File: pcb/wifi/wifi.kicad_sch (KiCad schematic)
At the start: 0 parts

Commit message: big components placed
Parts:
- added U1: ESP32-H2, PCM_Espressif:QFN-32-1EP_4x4mm_P0.4mm_EP2.9x2.9mm, symbol Espressif:ESP32-H2
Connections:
- new net: U1.1 (VDD3P3), U1.2 (VDD3P3), U1.27 (VDD3P3), U1.30 (VDD3P3), U1.31 (VDD3P3)
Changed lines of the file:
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@@
 	(generator_version "10.0")
 	(paper "A4")
+	(symbol
+		(lib_id "Espressif:ESP32-H2")
+		(at 57.15 55.88 0)
+		(unit 1)
+		(body_style 1)
+		(exclude_from_sim no)
+		(in_bom yes)
+		(on_board yes)
+		(in_pos_files yes)
+		(dnp no)
+		(fields_autoplaced yes)
+		(property "Reference" "U1"
+			(at 59.2933 83.82 0)
+			(show_name no)
+			(do_not_autoplace no)
+			(effects
+				(font
+					(size 1.27 1.27)
+				)
+				(justify left)
+			)
+		)
+		(property "Value" "ESP32-H2"
+			(at 59.2933 86.36 0)
+			(show_name no)
+			(do_not_autoplace no)
+			(effects
+				(font
+					(size 1.27 1.27)
+				)
+				(justify left)
+			)
+		)
+		(property "Footprint" "PCM_Espressif:QFN-32-1EP_4x4mm_P0.4mm_EP2.9x2.9mm"
+			(at 57.15 95.25 0)
+			(hide yes)
+			(show_name no)
+			(do_not_autoplace no)
+			(effects
+				(font
+					(size 1.27 1.27)
+				)
+			)
+		)
+		(property "Datasheet" "https://www.espressif.com/sites/default/files/documentation/esp32-h2_datasheet_en.pdf"
+			(at 57.15 97.79 0)
+			(hide yes)
+			(show_name no)
+			(do_not_autoplace no)
+			(effects
+				(font
+					(size 1.27 1.27)
+				)
+			)
+		)
+		(property "Description" "ESP32-H2, ultra-low-power SoC with RISC-V single-core microprocessor,Bluetooth 5 (LE), Zigbee and Thread (802.15.4),QFN-32"
+			(at 57.15 55.88 0)
+			(hide yes)
+			(show_name no)
+			(do_not_autoplace no)
+			(effects
+				(font
+					(size 1.27 1.27)
+				)
+			)
+		)
+		(pin "21"
+		)
+		(pin "12"
+		)
+		(pin "16"
+		)
+		(pin "26"
+		)
+		(pin "13"
+		)
+		(pin "33"
+		)
+		(pin "24"
+		)
+		(pin "14"
+		)
+		(pin "1"
+		)
+		(pin "3"
+		)
+		(pin "4"
+		)
+		(pin "7"
+		)
+		(pin "6"
+		)
+		(pin "2"
+		)
+		(pin "10"
+		)
+		(pin "8"
+		)
+		(pin "27"
+		)
+		(pin "28"
+		)
+		(pin "15"
+		)
+		(pin "30"
+		)
+		(pin "20"
+		)
+		(pin "22"
+		)
+		(pin "29"
+		)
+		(pin "19"
+		)
+		(pin "9"
+		)
+		(pin "17"
+		)
+		(pin "11"
+		)
+		(pin "23"
+		)
+		(pin "18"
+		)
+		(pin "25"
+		)
+		(pin "31"
+		)
+		(pin "32"
+		)
+		(pin "5"
+		)
+		(instances
+			(project "wifi"
+				(path "/cab5c3ac-9821-4913-9e7a-554539370212"
+					(reference "U1")
+					(unit 1)
+				)
+			)
+		)
+	)
 	(sheet_instances
 		(path "/"

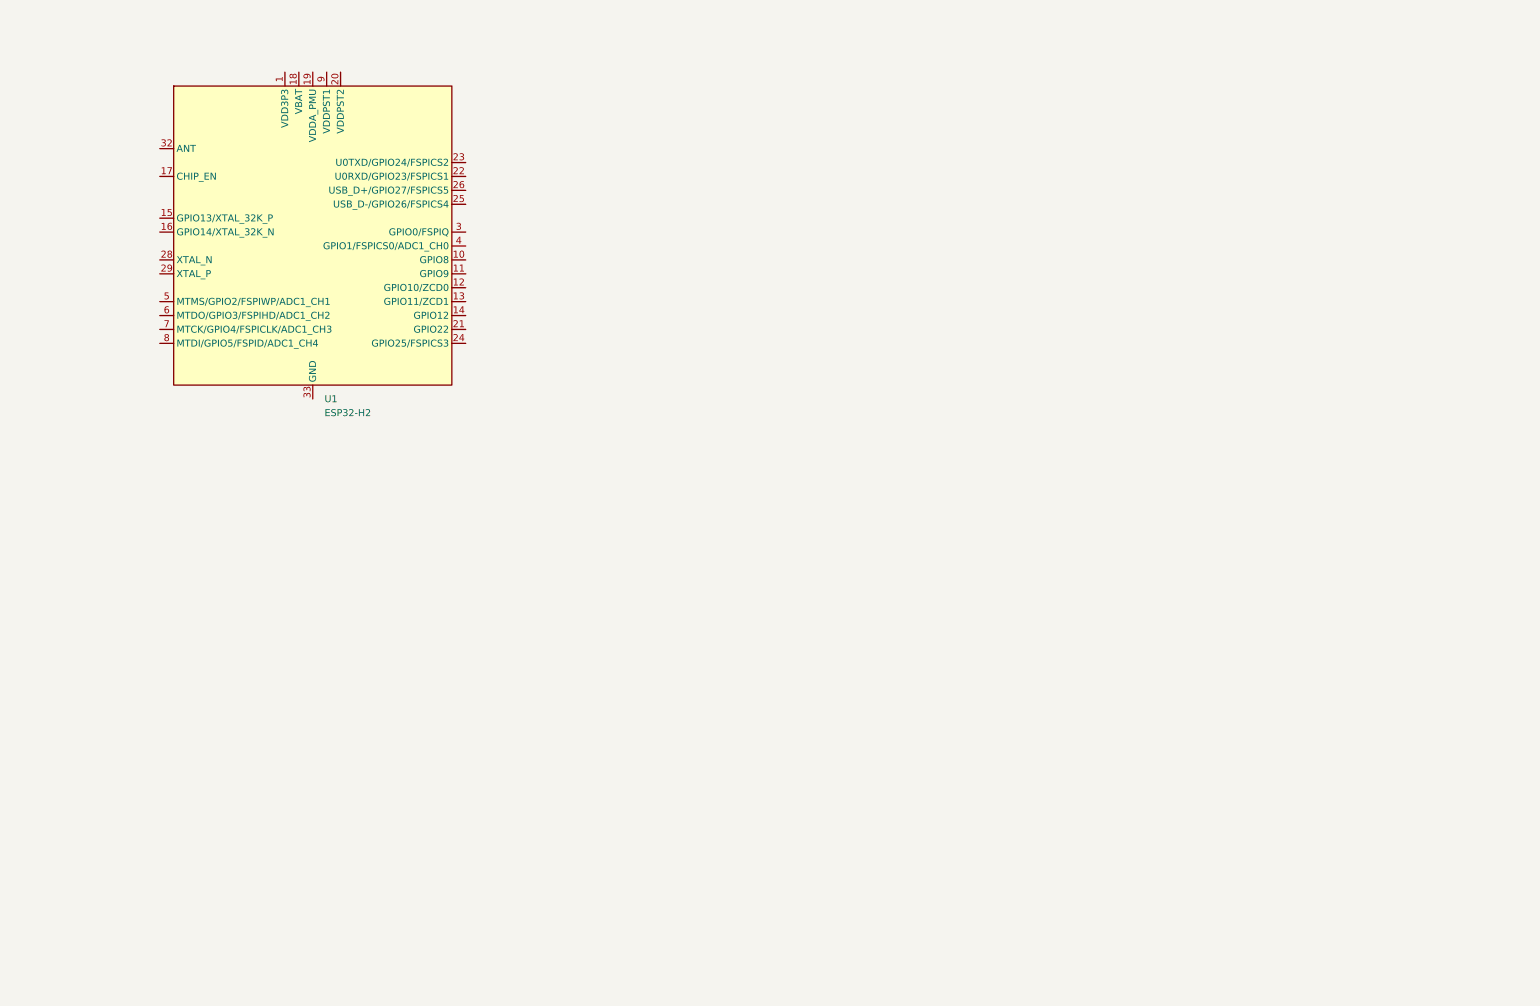
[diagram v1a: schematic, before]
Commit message: added components for esp32-h2 for the most part; gpio needs fill in and same with solving vdd3p3 issue.
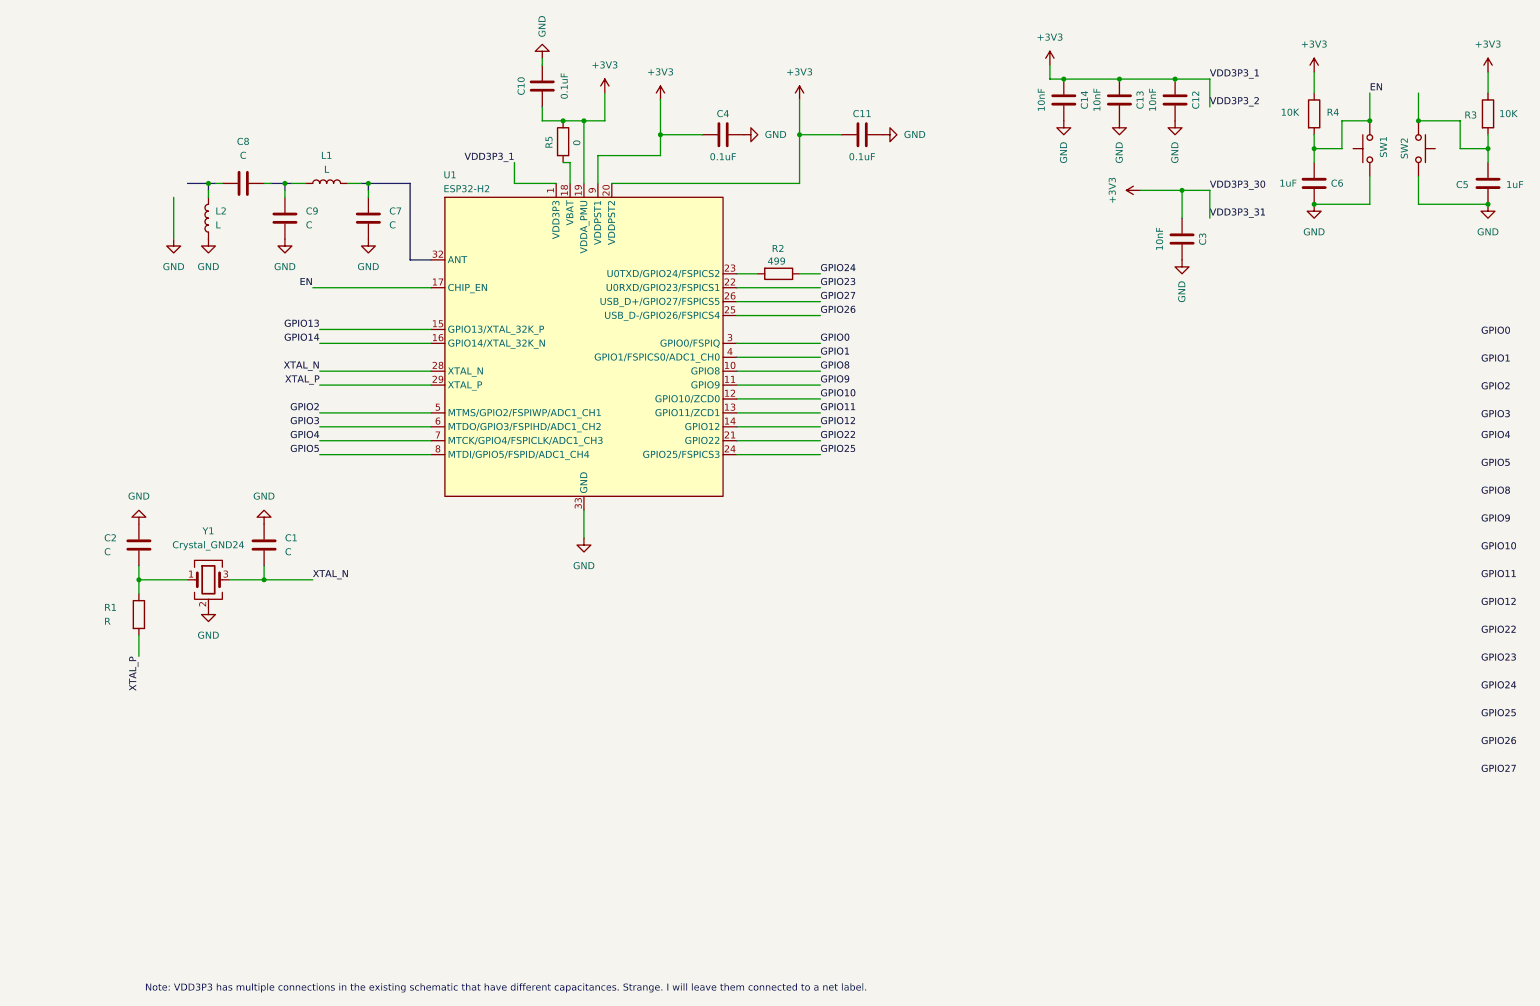
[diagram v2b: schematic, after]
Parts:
- added C1, C2, C7, C8, C9: C, symbol Device:C
- added C10, C11, C4: 0.1uF, symbol Device:C
- added C12, C13, C14, C3: 10nF, symbol Device:C
- added C5, C6: 1uF, symbol Device:C
- added L1, L2: L, symbol Device:L
- added R1: R, symbol Device:R
- added R2: 499, symbol Device:R
- added R3, R4: 10K, symbol Device:R
- added R5: 0, symbol Device:R
- added SW1, SW2: SW_Push, symbol Switch:SW_Push
- added Y1: Crystal_GND24, Crystal:Crystal_SMD_2016-4Pin_2.0x1.6mm, symbol Device:Crystal_GND24
- U1: footprint PCM_Espressif:QFN-32-1EP_4x4mm_P0.4mm_EP2.9x2.9mm -> Espressif:QFN-32-1EP_4x4mm_P0.4mm_EP2.9x2.9mm
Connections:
- net +3V3: now reaches U1.1 (VDD3P3), U1.2 (VDD3P3), U1.27 (VDD3P3), U1.30 (VDD3P3), U1.31 (VDD3P3)
- net +3V3: now also U1.19 (VDDA_PMU), U1.20 (VDDPST2), U1.9 (VDDPST1), C10.2, C11.2, C12.2, C13.2, C14.2, C3.2, C4.2, R3.1, R4.1, R5.1
- net GPIO8: now reaches U1.10 (GPIO8)
- net GPIO9: now reaches U1.11 (GPIO9)
- net GPIO10: now reaches U1.12 (GPIO10/ZCD0)
- net GPIO11: now reaches U1.13 (GPIO11/ZCD1)
- net GPIO12: now reaches U1.14 (GPIO12)
- net GPIO13: now reaches U1.15 (GPIO13/XTAL_32K_P)
- net GPIO14: now reaches U1.16 (GPIO14/XTAL_32K_N)
- net EN: now reaches U1.17 (CHIP_EN)
- net EN: now also C6.1, R4.2, SW1.2
- net at U1.18 (VBAT): now also R5.2
- net GPIO22: now reaches U1.21 (GPIO22)
- net GPIO23: now reaches U1.22 (U0RXD/GPIO23/FSPICS1)
- net at U1.23 (U0TXD/GPIO24/FSPICS2): now also R2.2
- net GPIO25: now reaches U1.24 (GPIO25/FSPICS3)
- net GPIO26: now reaches U1.25 (USB_D-/GPIO26/FSPICS4)
- net GPIO27: now reaches U1.26 (USB_D+/GPIO27/FSPICS5)
- net XTAL_N: now reaches U1.28 (XTAL_N)
- net XTAL_N: now also C1.2, Y1.3
- net XTAL_P: now reaches U1.29 (XTAL_P)
- net XTAL_P: now also R1.2
- net GPIO0: now reaches U1.3 (GPIO0/FSPIQ)
- net GND: now reaches U1.33 (GND)
- net GND: now also C1.1, C10.1, C11.1, C12.1, C13.1, C14.1, C2.1, C3.1, C4.1, C5.2, C6.2, C7.2, C9.2, L2.1, SW1.1, SW2.2, Y1.2 (G), Y1.4 (G)
- net GPIO1: now reaches U1.4 (GPIO1/FSPICS0/ADC1_CH0)
- net GPIO2: now reaches U1.5 (MTMS/GPIO2/FSPIWP/ADC1_CH1)
- net GPIO3: now reaches U1.6 (MTDO/GPIO3/FSPIHD/ADC1_CH2)
- net GPIO4: now reaches U1.7 (MTCK/GPIO4/FSPICLK/ADC1_CH3)
- net GPIO5: now reaches U1.8 (MTDI/GPIO5/FSPID/ADC1_CH4)
- new net: C2.2, R1.1, Y1.1
- new net: C5.1, R3.2, SW2.1
- new net GPIO24: R2.1
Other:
- note added: "Note: VDD3P3 has multiple connections in the existing schematic that have different capacitances. Strange. I will leave them connected to a net label."
- moved on the sheet: U1

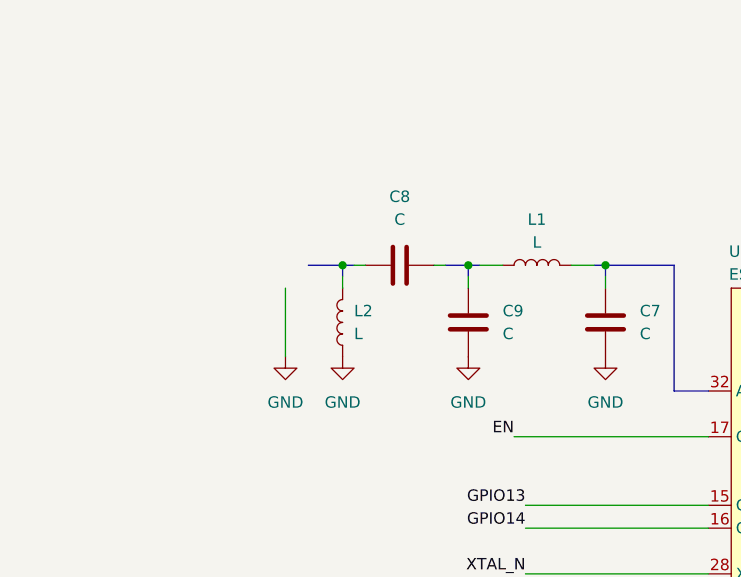
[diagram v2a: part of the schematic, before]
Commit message: Added AN043 Antenna
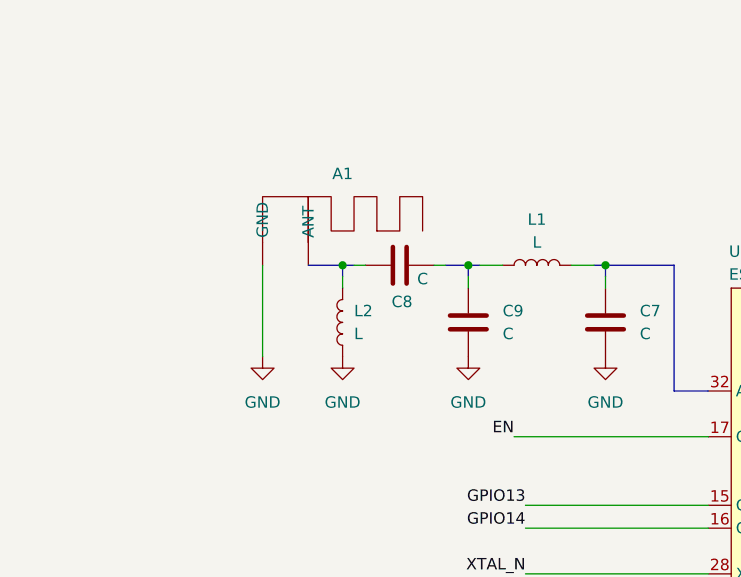
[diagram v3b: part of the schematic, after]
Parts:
- added A1: (no value), esp_wifi:ANT_MIFA_TI_AN043, symbol New_Library:AN043
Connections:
- net GND: now also A1. (ANT)
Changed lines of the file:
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@@
 	(wire
 		(pts
+			(xy 29.21 44.45) (xy 29.21 54.61)
+		)
+		(stroke
+			(width 0)
+			(type default)
+		)
+	)
+	(wire
+		(pts
 			(xy 271.78 35.56) (xy 271.78 38.1)
 		)
@@
 	(wire
 		(pts
-			(xy 31.75 46.99) (xy 31.75 54.61)
-		)
-		(stroke
-			(width 0)
-			(type default)
-		)
-	)
-	(wire
-		(pts
 			(xy 25.4 116.84) (xy 34.29 116.84)
 		)
@@
 	(symbol
 		(lib_id "power:GND")
-		(at 31.75 54.61 0)
+		(at 29.21 54.61 0)
 		(unit 1)
 		(body_style 1)
@@
 		(fields_autoplaced yes)
 		(property "Reference" "#PWR016"
-			(at 31.75 60.96 0)
+			(at 29.21 60.96 0)
 			(hide yes)
 			(show_name no)
@@
 		)
 		(property "Value" "GND"
-			(at 31.75 59.69 0)
+			(at 29.21 59.69 0)
 			(show_name no)
 			(do_not_autoplace no)
@@
 		)
 		(property "Footprint" ""
-			(at 31.75 54.61 0)
+			(at 29.21 54.61 0)
 			(hide yes)
 			(show_name no)
@@
 		)
 		(property "Datasheet" ""
-			(at 31.75 54.61 0)
+			(at 29.21 54.61 0)
 			(hide yes)
 			(show_name no)
@@
 		)
 		(property "Description" "Power symbol creates a global label with name \"GND\" , ground"
-			(at 31.75 54.61 0)
+			(at 29.21 54.61 0)
 			(hide yes)
 			(show_name no)
@@
 		(in_pos_files yes)
 		(dnp no)
-		(fields_autoplaced yes)
 		(property "Reference" "C8"
-			(at 44.45 36.83 90)
+			(at 44.704 48.514 90)
 			(show_name no)
 			(do_not_autoplace no)
@@
 		)
 		(property "Value" "C"
-			(at 44.45 39.37 90)
+			(at 46.99 45.974 90)
 			(show_name no)
 			(do_not_autoplace no)
@@
 					(unit 1)
 				)
+			)
+		)
+	)
+	(symbol
+		(lib_id "New_Library:AN043")
+		(at 31.75 40.64 0)
+		(unit 1)
+		(body_style 1)
+		(exclude_from_sim no)
+		(in_bom yes)
+		(on_board yes)
+		(in_pos_files yes)
+		(dnp no)
+		(fields_autoplaced yes)
+		(property "Reference" "A1"
+			(at 38.1 34.29 0)
+			(show_name no)
+			(do_not_autoplace no)
+			(effects
+				(font
+					(size 1.27 1.27)
+				)
+			)
+		)
+		(property "Value" ""
+			(at 31.75 40.64 0)
+			(show_name no)
+			(do_not_autoplace no)
+			(effects
+				(font
+					(size 1.27 1.27)
+				)
+			)
+		)
+		(property "Footprint" "esp_wifi:ANT_MIFA_TI_AN043"
+			(at 31.75 40.64 0)
+			(hide yes)
+			(show_name no)
+			(do_not_autoplace no)
+			(effects
+				(font
+					(size 1.27 1.27)
+				)
+			)
+		)
+		(property "Datasheet" ""
+			(at 31.75 40.64 0)
+			(hide yes)
+			(show_name no)
+			(do_not_autoplace no)
+			(effects
+				(font
+					(size 1.27 1.27)
+				)
+			)
+		)
+		(property "Description" ""
+			(at 31.75 40.64 0)
+			(hide yes)
+			(show_name no)
+			(do_not_autoplace no)
+			(effects
+				(font
+					(size 1.27 1.27)
+				)
+			)
+		)
+		(pin ""
+		)
+		(pin ""
+		)
+		(instances
+			(project "wifi"
+				(path "/cab5c3ac-9821-4913-9e7a-554539370212"
+					(reference "A1")
+					(unit 1)
+				)
